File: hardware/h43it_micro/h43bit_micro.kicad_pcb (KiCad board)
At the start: 2 copper layers, 1 part, among them U1 ATtiny414-SS

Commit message: first draft of schematic
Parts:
- added J1: Conn_01x04_Pin, Connector_PinHeader_2.54mm:PinHeader_1x04_P2.54mm_Vertical, F.Cu at (152.4, 83.8)
- added SW1: SW_Push, MyLib:PTS526 SM15 SMTR2 LFS, F.Cu at (141.8, 87.0)
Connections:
- U1 pad 1: unconnected-(U1-VCC-Pad1) -> VCC
- U1 pad 10: unconnected-(U1-~{RESET}/PA0-Pad10) -> /UPDI
- U1 pad 11: unconnected-(U1-PA1-Pad11) -> /L-
- U1 pad 12: unconnected-(U1-PA2-Pad12) -> /M-
- U1 pad 13: unconnected-(U1-PA3-Pad13) -> /N-
- U1 pad 14: unconnected-(U1-GND-Pad14) -> GND
- U1 pad 2: unconnected-(U1-PA4-Pad2) -> /O-
- U1 pad 4: unconnected-(U1-PA6-Pad4) -> /D+
- U1 pad 5: unconnected-(U1-PA7-Pad5) -> /SW
- U1 pad 6: unconnected-(U1-PB3-Pad6) -> /C+
- U1 pad 7: unconnected-(U1-PB2-Pad7) -> /TX
- U1 pad 8: unconnected-(U1-PB1-Pad8) -> /B+
- U1 pad 9: unconnected-(U1-PB0-Pad9) -> /A+

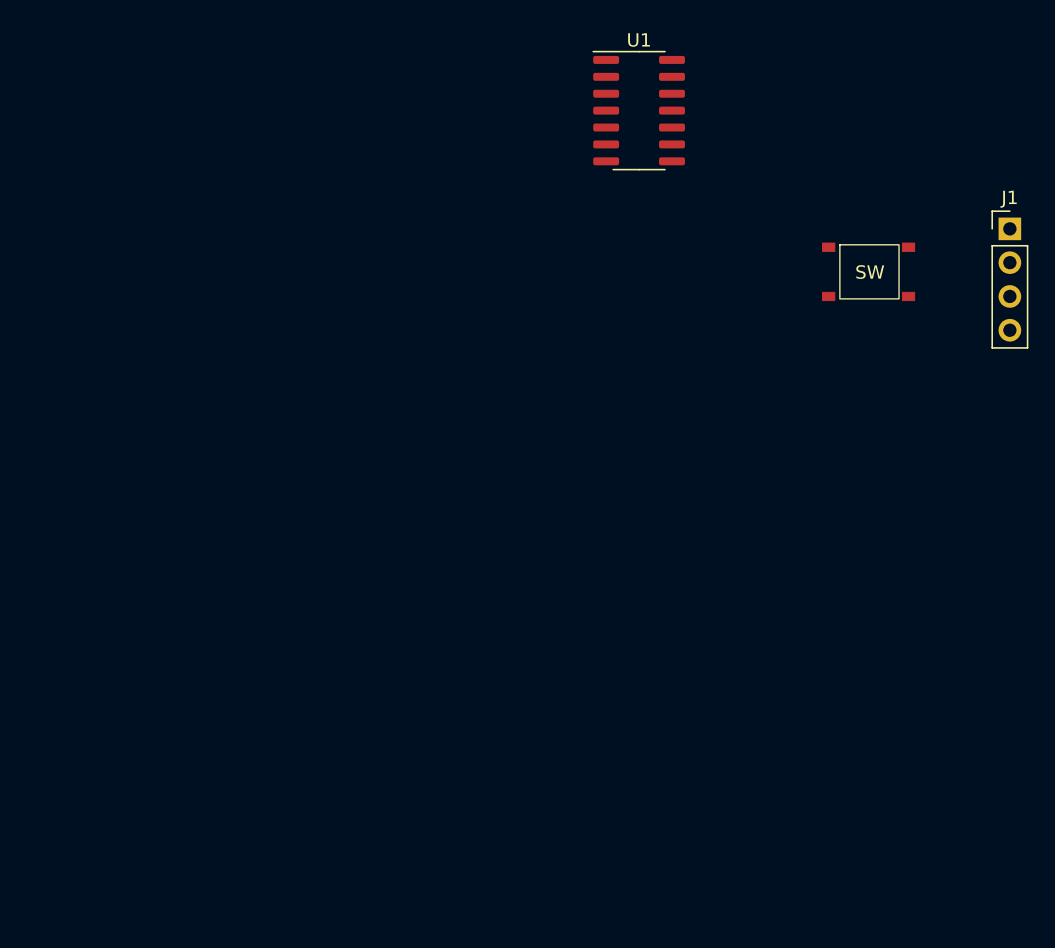
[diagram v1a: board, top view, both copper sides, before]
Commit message: draft of a circular micro
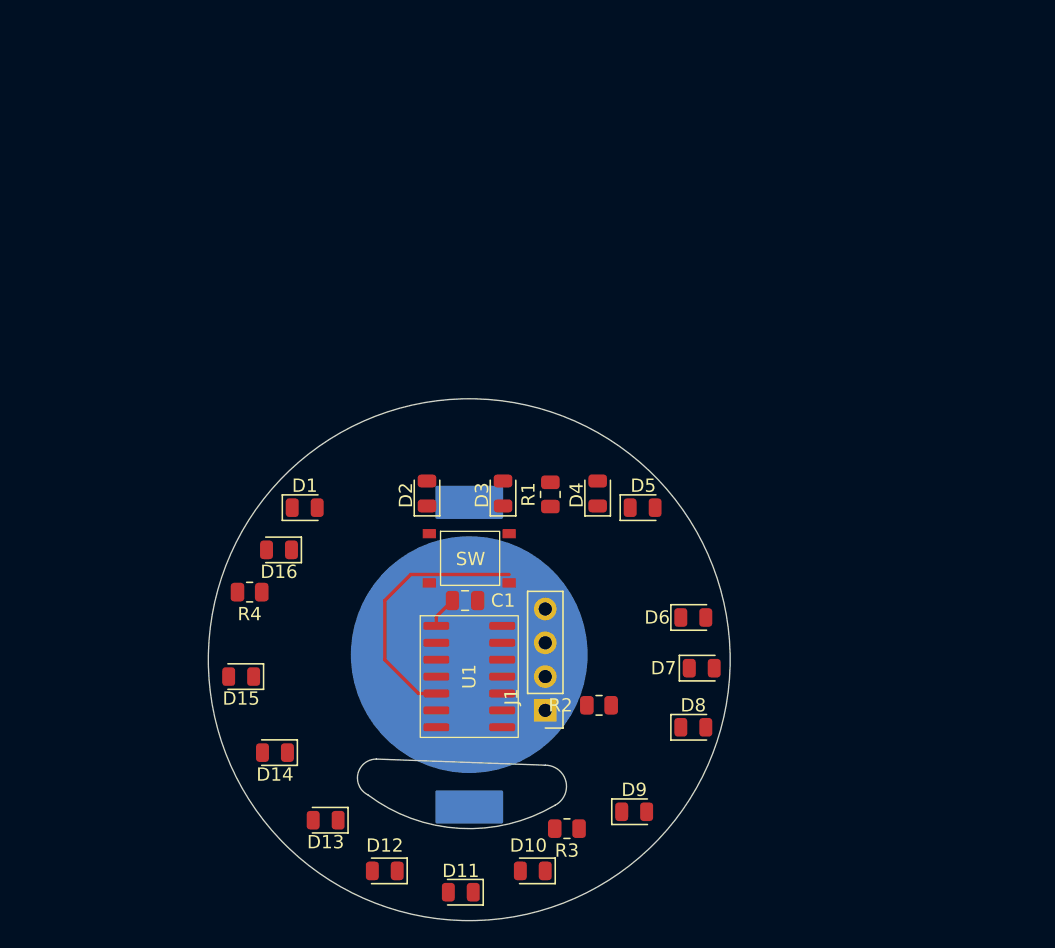
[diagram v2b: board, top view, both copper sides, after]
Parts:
- added BT1: Battery_Cell, MyLib:BAT-HLD-001, B.Cu at (111.8, 115.8)
- added C1: 1uF, Capacitor_SMD:C_0805_2012Metric, F.Cu at (111.4, 111.8)
- added D1: LED, LED_SMD:LED_0805_2012Metric, F.Cu at (99.4, 104.8)
- added D10: LED, LED_SMD:LED_0805_2012Metric, F.Cu at (116.5, 132.1)
- added D11: LED, LED_SMD:LED_0805_2012Metric, F.Cu at (111.1, 133.7)
- added D12: LED, LED_SMD:LED_0805_2012Metric, F.Cu at (105.4, 132.1)
- added D13: LED, LED_SMD:LED_0805_2012Metric, F.Cu at (101.0, 128.3)
- added D14: LED, LED_SMD:LED_0805_2012Metric, F.Cu at (97.2, 123.2)
- added D15: LED, LED_SMD:LED_0805_2012Metric, F.Cu at (94.6, 117.5)
- added D16: LED, LED_SMD:LED_0805_2012Metric, F.Cu at (97.5, 108.0)
- added D2: LED, LED_SMD:LED_0805_2012Metric, F.Cu at (108.6, 103.7)
- added D3: LED, LED_SMD:LED_0805_2012Metric, F.Cu at (114.3, 103.7)
- added D4: LED, LED_SMD:LED_0805_2012Metric, F.Cu at (121.4, 103.7)
- added D5: LED, LED_SMD:LED_0805_2012Metric, F.Cu at (124.8, 104.8)
- added D6: LED, LED_SMD:LED_0805_2012Metric, F.Cu at (128.6, 113.0)
- added D7: LED, LED_SMD:LED_0805_2012Metric, F.Cu at (129.2, 116.8)
- added D8: LED, LED_SMD:LED_0805_2012Metric, F.Cu at (128.6, 121.3)
- added D9: LED, LED_SMD:LED_0805_2012Metric, F.Cu at (124.2, 127.6)
- added R1: 27Ω, Resistor_SMD:R_0805_2012Metric, F.Cu at (117.9, 103.8)
- added R2: 27Ω, Resistor_SMD:R_0805_2012Metric, F.Cu at (121.5, 119.6)
- added R3: 27Ω, Resistor_SMD:R_0805_2012Metric, F.Cu at (119.1, 128.9)
- added R4: 27Ω, Resistor_SMD:R_0805_2012Metric, F.Cu at (95.2, 111.1)
- moved J1 50.3 mm to (117.5, 120.0), turned to 180 degrees
- moved U1 44.4 mm to (111.8, 117.5)
- moved SW1 36.9 mm to (111.8, 108.6)
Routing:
- net /SW: track 0.00 -> 19.5 mm
- net VCC: track 0.00 -> 2.41 mm
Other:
- board outline added: 39.2 x 39.2 mm

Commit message: circular tracks
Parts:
- moved D13 34.2 mm to (81.8, 100.0)
- moved D12 33.6 mm to (83.2, 106.9), turned to -157.5 degrees
- moved D14 33.2 mm to (83.2, 93.1), turned to 157.5 degrees
- moved R3 32.0 mm to (91.9, 112.0), turned to -125 degrees
- moved D11 31.9 mm to (87.1, 112.7), turned to -135 degrees
- moved D15 31.2 mm to (87.1, 87.2), turned to 135 degrees
- moved D10 28.2 mm to (92.9, 116.6), turned to -112.5 degrees
- moved D9 26.2 mm to (99.8, 118.0), turned to -90 degrees
- moved J1 26.0 mm to (111.5, 94.7), turned to 0 degrees
- moved D16 25.0 mm to (92.9, 83.3), turned to 112.5 degrees
- moved R4 24.0 mm to (91.7, 87.4), turned to 130 degrees
- moved D1 22.8 mm to (99.8, 82.0), turned to 90 degrees
- moved D8 22.4 mm to (106.7, 116.6), turned to -67.5 degrees
- moved C1 20.8 mm to (101.5, 93.5)
- moved D2 20.5 mm to (106.7, 83.3), turned to 67.5 degrees
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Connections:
- BT1 pad 1: VCC -> /N-
- BT1 pad 2: GND -> /N-
- D1 pad 1: /M- -> /N-
- D5 pad 1: /M- -> /N-
- U1 pad 12: /M- -> /N-
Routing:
- net /N-: track 0.00 -> 122.5 mm, vias 0 -> 3
- net Net-(D1-A): track 0.00 -> 26.2 mm
- net Net-(D5-A): track 0.00 -> 25.9 mm
- net Net-(D10-A): track 0.00 -> 25.8 mm
- net Net-(D13-A): track 0.00 -> 25.5 mm
- net /SW: track 19.5 -> 0.00 mm
- net VCC: track 2.41 -> 4.05 mm
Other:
- board size 39.2 x 39.2 mm -> 40 x 40 mm

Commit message: filled area
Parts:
- U1: footprint Package_SO:SOIC-14_3.9x8.7mm_P1.27mm -> MyLib:SOIC-14_3.9x8.7mm_P1.27mm
- moved U1 1.96 mm to (101.1, 98.0)
- moved C1 1.47 mm to (101.5, 92.0)
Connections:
- BT1 pad 1: /N- -> VCC
- BT1 pad 2: /N- -> GND
- D1 pad 1: /N- -> /M-
- D5 pad 1: /N- -> /M-
- U1 pad 11: /L- -> /M-
- U1 pad 13: /N- -> /O-
- U1 pad 2: /O- -> /P-
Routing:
- net /P-: track 0.00 -> 77.0 mm, vias 0 -> 4
- net /M-: track 0.00 -> 75.4 mm, vias 0 -> 4
- net /O-: track 0.00 -> 74.9 mm, vias 0 -> 5
- net /N-: track 122.5 -> 75.9 mm, vias 3 -> 4
- net VCC: track 4.05 -> 42.2 mm, vias 0 -> 2
- net /TX: track 0.00 -> 31.2 mm, vias 0 -> 2
- net /A+: track 0.00 -> 29.3 mm, vias 0 -> 2
- net /D+: track 0.00 -> 13.8 mm
- net /C+: track 0.00 -> 13.8 mm
- net /B+: track 0.00 -> 9.49 mm
- net /UPDI: track 0.00 -> 9.20 mm
- net /SW: track 0.00 -> 6.00 mm
- added copper zone on B.Cu, net GND
- added copper zone on F.Cu, net GND
